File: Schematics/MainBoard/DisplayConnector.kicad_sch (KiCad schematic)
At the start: 11 parts, among them J5 Conn_02x20_Odd_Even, U8 TXS0108, U9 TXS0108

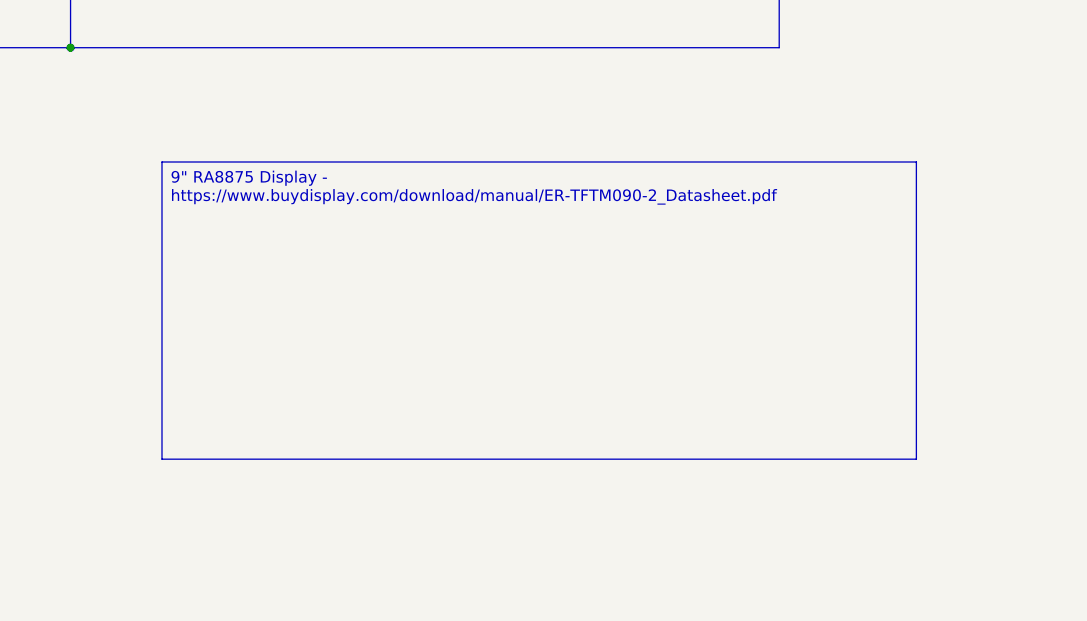
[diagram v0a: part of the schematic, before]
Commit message: Updated USB wiring, moved key parts, increased board dimensions
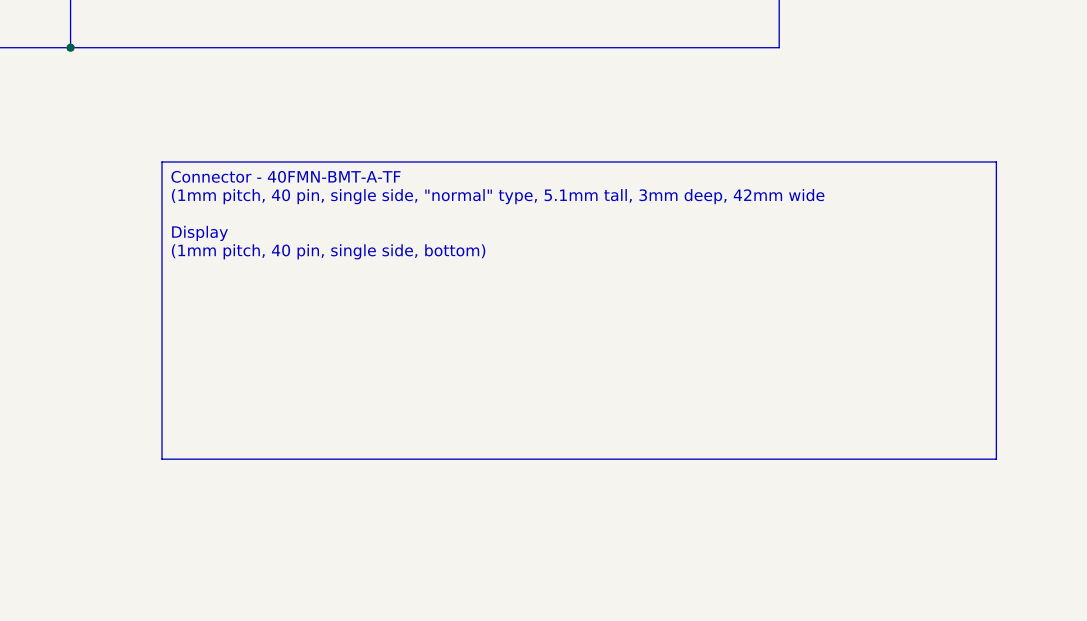
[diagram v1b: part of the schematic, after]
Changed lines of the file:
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@@
 	(generator_version "9.0")
 	(paper "A4")
-	(text_box "9\" RA8875 Display - https://www.buydisplay.com/download/manual/ER-TFTM090-2_Datasheet.pdf"
+	(text_box "Connector - 40FMN-BMT-A-TF\n   (1mm pitch, 40 pin, single side, \"normal\" type, 5.1mm tall, 3mm deep, 42mm wide\n\nDisplay\n   (1mm pitch, 40 pin, single side, bottom)"
 		(exclude_from_sim no)
 		(at 165.1 129.54 0)
-		(size 83.82 33.02)
+		(size 92.71 33.02)
 		(margins 0.9525 0.9525 0.9525 0.9525)
 		(stroke

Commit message: rough placement of parts to help with 3D CAD
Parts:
- J5: footprint Connector_PinHeader_2.54mm:PinHeader_2x20_P2.54mm_Vertical -> FFC3B07-40-T:GCT_FFC3B07-40-T
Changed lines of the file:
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@@
 			)
 		)
-		(property "Footprint" "Connector_PinHeader_2.54mm:PinHeader_2x20_P2.54mm_Vertical"
+		(property "Footprint" "FFC3B07-40-T:GCT_FFC3B07-40-T"
 			(at 193.04 71.12 0)
 			(effects

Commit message: Work on PCB
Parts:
- C35, C36, C51, C52: footprint Capacitor_SMD:C_0603_1608Metric -> Capacitor_SMD:C_0402_1005Metric
- R91, R92: footprint Resistor_SMD:R_0603_1608Metric -> Resistor_SMD:R_0402_1005Metric
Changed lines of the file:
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@@
 			)
 		)
-		(property "Footprint" "Capacitor_SMD:C_0603_1608Metric"
+		(property "Footprint" "Capacitor_SMD:C_0402_1005Metric"
 			(at 89.8652 182.88 0)
 			(effects
@@
 			)
 		)
-		(property "Footprint" "Capacitor_SMD:C_0603_1608Metric"
+		(property "Footprint" "Capacitor_SMD:C_0402_1005Metric"
 			(at 80.3148 182.88 0)
 			(effects
@@
 			)
 		)
-		(property "Footprint" "Capacitor_SMD:C_0603_1608Metric"
+		(property "Footprint" "Capacitor_SMD:C_0402_1005Metric"
 			(at 122.8852 182.88 0)
 			(effects
@@
 			)
 		)
-		(property "Footprint" "Resistor_SMD:R_0603_1608Metric"
+		(property "Footprint" "Resistor_SMD:R_0402_1005Metric"
 			(at 121.412 97.79 90)
 			(effects
@@
 			)
 		)
-		(property "Footprint" "Resistor_SMD:R_0603_1608Metric"
+		(property "Footprint" "Resistor_SMD:R_0402_1005Metric"
 			(at 121.412 107.95 90)
 			(effects
@@
 			)
 		)
-		(property "Footprint" "Capacitor_SMD:C_0603_1608Metric"
+		(property "Footprint" "Capacitor_SMD:C_0402_1005Metric"
 			(at 113.3348 182.88 0)
 			(effects

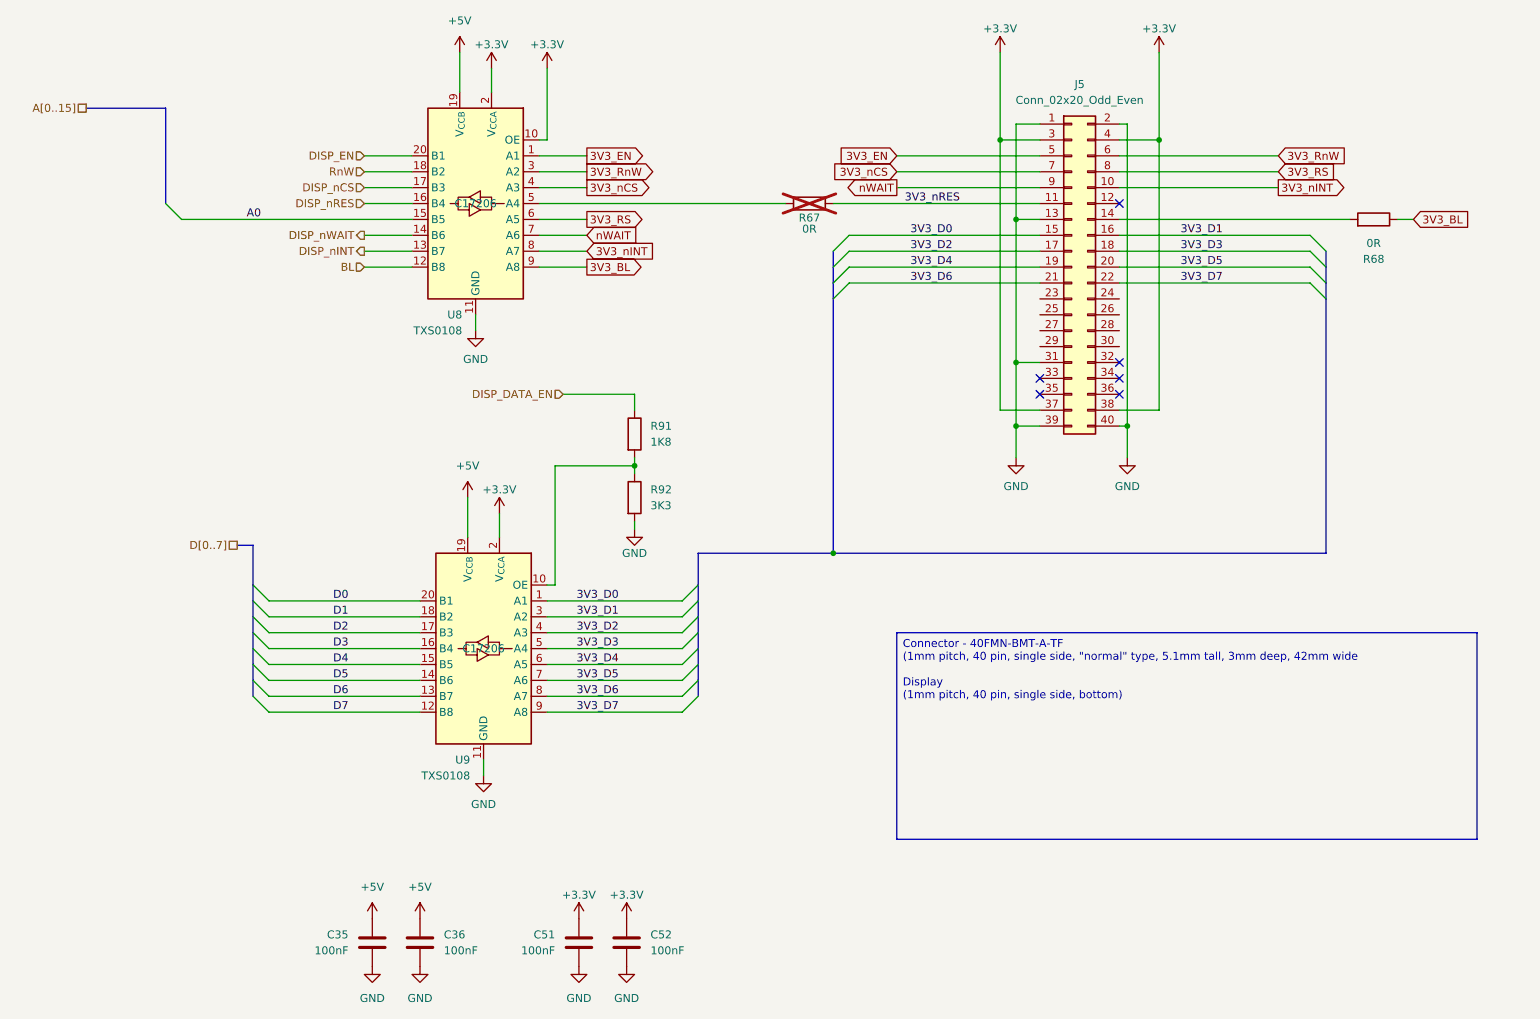
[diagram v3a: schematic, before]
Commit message: Work on PCB routing, added SwinSID
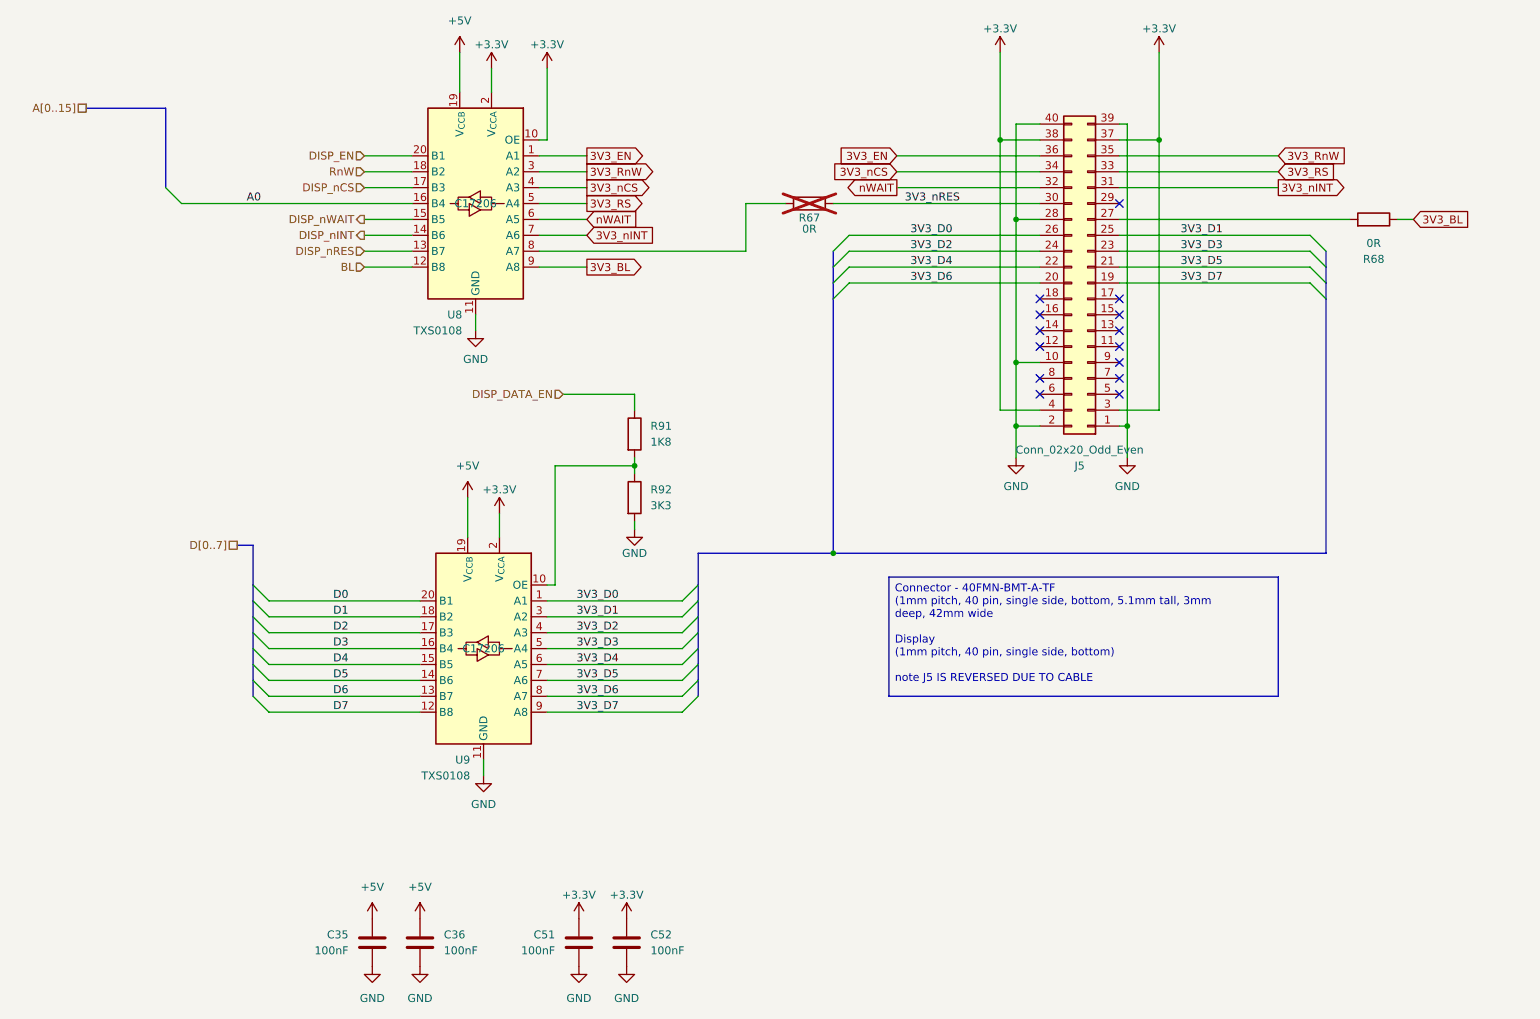
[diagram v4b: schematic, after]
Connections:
- net 3V3_D0: now also J5.26 (Pin_26); no longer J5.15 (Pin_15)
- net 3V3_D1: now also J5.25 (Pin_25); no longer J5.16 (Pin_16)
- net 3V3_D2: now also J5.24 (Pin_24); no longer J5.17 (Pin_17)
- net 3V3_D3: now also J5.23 (Pin_23); no longer J5.18 (Pin_18)
- net 3V3_D4: now also J5.22 (Pin_22); no longer J5.19 (Pin_19)
- net 3V3_D5: now also J5.21 (Pin_21); no longer J5.20 (Pin_20)
- net 3V3_D6: now also J5.20 (Pin_20); no longer J5.21 (Pin_21)
- net 3V3_D7: now also J5.19 (Pin_19); no longer J5.22 (Pin_22)
- net 3V3_EN: now also J5.36 (Pin_36); no longer J5.5 (Pin_5)
- net 3V3_RS: now also J5.33 (Pin_33), U8.5 (A4); no longer J5.8 (Pin_8), U8.6 (A5)
- net 3V3_RnW: now also J5.35 (Pin_35); no longer J5.6 (Pin_6)
- net 3V3_nCS: now also J5.34 (Pin_34); no longer J5.7 (Pin_7)
- net 3V3_nINT: now also J5.31 (Pin_31), U8.7 (A6); no longer J5.10 (Pin_10), U8.8 (A7)
- net 3V3_nRES: now also J5.30 (Pin_30); no longer J5.11 (Pin_11)
- net A0: now also U8.16 (B4); no longer U8.15 (B5)
- net DISP_nINT: now also U8.14 (B6); no longer U8.13 (B7)
- net DISP_nRES: now also U8.13 (B7); no longer U8.16 (B4)
- net DISP_nWAIT: now also U8.15 (B5); no longer U8.14 (B6)
- net GND: now also J5.10 (Pin_10), J5.28 (Pin_28); no longer J5.13 (Pin_13), J5.31 (Pin_31)
- net nWAIT: now also J5.32 (Pin_32), U8.6 (A5); no longer J5.9 (Pin_9), U8.7 (A6)
- net at R67.1: now also U8.8 (A7); no longer U8.5 (A4)
- net at J5.14 (Pin_14): no longer R68.2
- net at J5.27 (Pin_27): now also R68.2
- no-connect marks 6 -> 14
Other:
- moved on the sheet: J5

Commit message: Updates based on production files for JLC
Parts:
- C35, C36, C51, C52: LCSC C113803 -> C307331
- J5: LCSC DNF -> C501492
- R68: now not fitted
- R91: LCSC C25890 -> C25871
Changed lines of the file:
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@@
 			)
 		)
-		(property "LCSC" "C113803"
+		(property "LCSC" "C307331"
 			(at 88.9 179.07 0)
 			(effects
@@
 			)
 		)
-		(property "LCSC" "DNF"
+		(property "LCSC" "C501492"
 			(at 195.58 73.66 0)
 			(effects
@@
 			)
 		)
-		(property "LCSC" "C113803"
+		(property "LCSC" "C307331"
 			(at 81.28 179.07 0)
 			(effects
@@
 			)
 		)
-		(property "LCSC" "C113803"
+		(property "LCSC" "C307331"
 			(at 121.92 179.07 0)
 			(effects
@@
 			)
 		)
-		(property "LCSC" "C25890"
+		(property "LCSC" "C25871"
 			(at 123.19 97.79 0)
 			(effects
@@
 		(in_bom yes)
 		(on_board yes)
-		(dnp no)
+		(dnp yes)
 		(property "Reference" "R68"
 			(at 241.3 69.85 90)
@@
 			)
 		)
-		(property "LCSC" "C113803"
+		(property "LCSC" "C307331"
 			(at 114.3 179.07 0)
 			(effects
